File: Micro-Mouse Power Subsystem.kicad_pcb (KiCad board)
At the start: 2 copper layers, 12 parts, among them J1 Pin Header, J2 TYPE-C-31-M-12

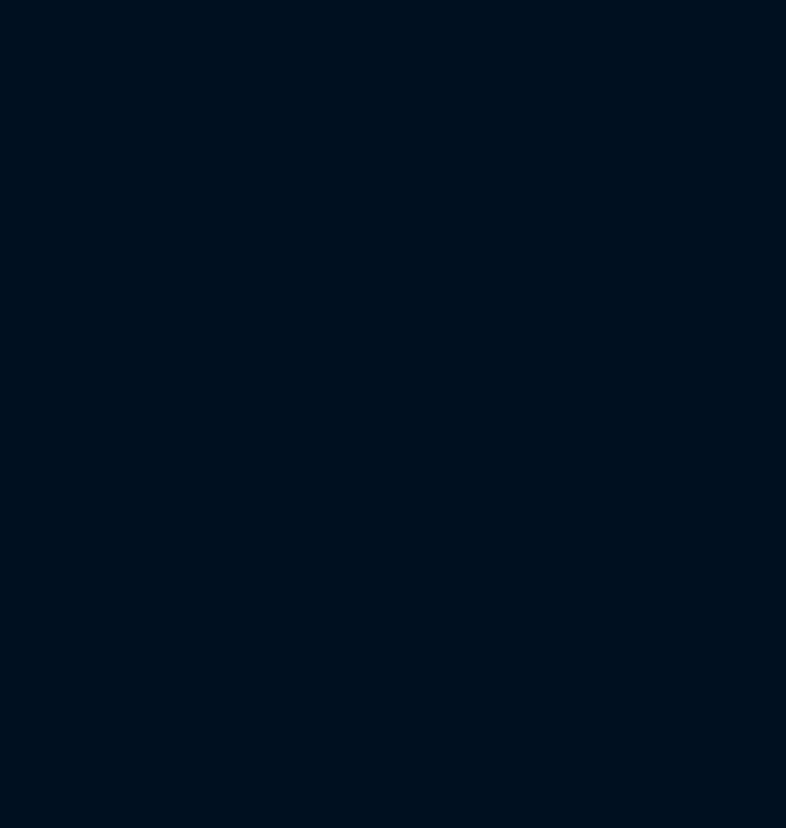
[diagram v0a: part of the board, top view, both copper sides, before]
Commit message: Updated PCB layout to include battery charging circuit
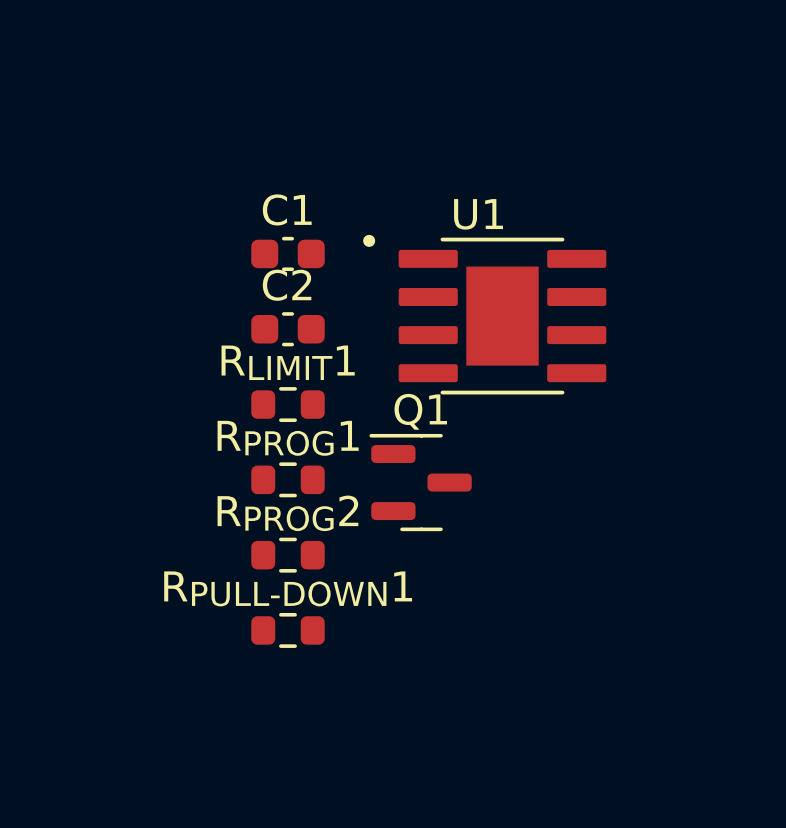
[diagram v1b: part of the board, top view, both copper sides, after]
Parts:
- added C1: C_{CHARGE_IN}, Capacitor_SMD:C_0603_1608Metric, F.Cu at (47.4, 94.0)
- added C2: C_Small, Capacitor_SMD:C_0603_1608Metric, F.Cu at (47.4, 96.5)
- added Q1: 2N7002, Package_TO_SOT_SMD:SOT-23, F.Cu at (51.9, 101.7)
- added R_{LIMIT}1: 1k, Resistor_SMD:R_0603_1608Metric, F.Cu at (47.4, 99.1)
- added R_{PROG}1: 6k, Resistor_SMD:R_0603_1608Metric, F.Cu at (47.4, 101.6)
- added R_{PROG}2: 3k, Resistor_SMD:R_0603_1608Metric, F.Cu at (47.4, 104.1)
- added R_{PULL-DOWN}1: 10k, Resistor_SMD:R_0603_1608Metric, F.Cu at (47.4, 106.6)
- added U1: TP4056, Imports:SOP127P600X175-9N, F.Cu at (54.6, 96.1)
